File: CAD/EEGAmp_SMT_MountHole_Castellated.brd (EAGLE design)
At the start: 19.9 x 11.2 mm, 16 parts, among them U1 TL084QD

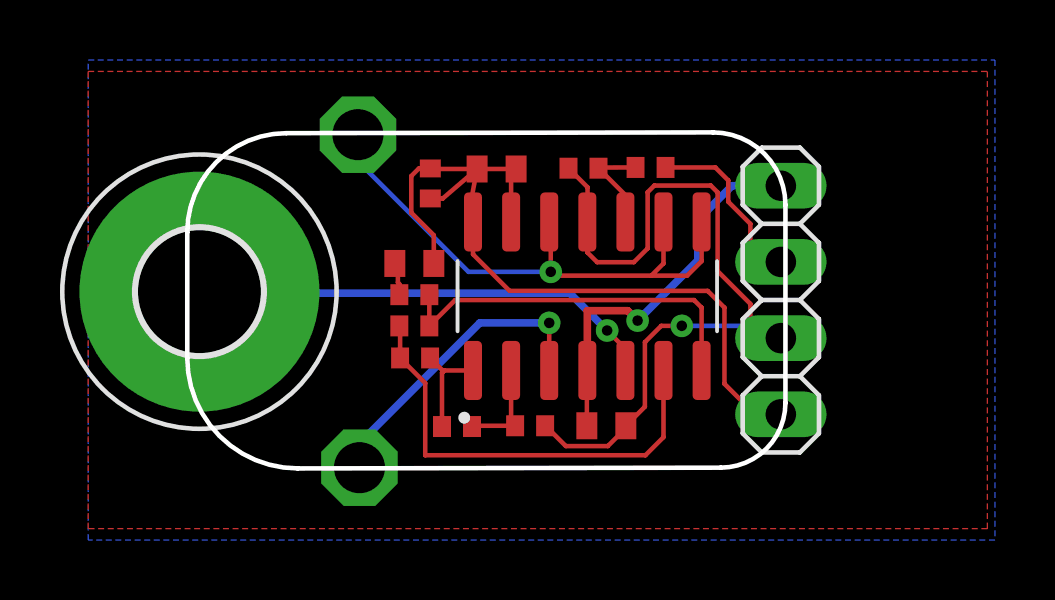
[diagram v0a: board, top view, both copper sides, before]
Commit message: added a filter cap on inputs
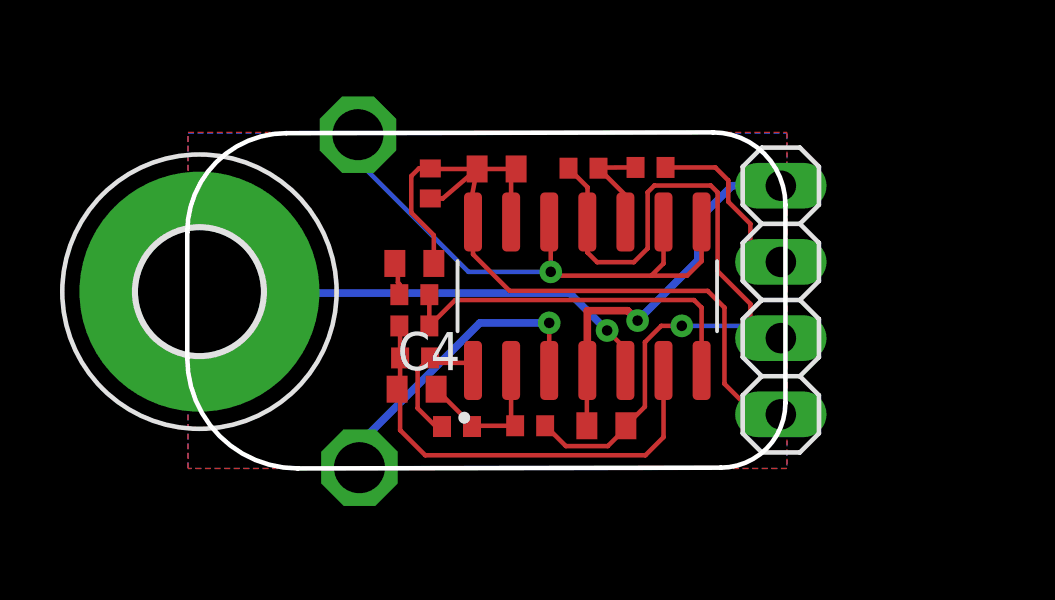
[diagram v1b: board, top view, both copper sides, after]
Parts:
- added C4: 2.2nF, rcl:C0402
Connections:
- net 1IN-: now also C4.2
- net 2IN-: now also C4.1
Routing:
- net 1IN-: track 3.36 -> 5.08 mm
- net 1OUT: track 3.49 -> 4.52 mm
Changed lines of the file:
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@@
 <attribute name="VALUE" x="26.7716" y="48.8188" size="0.0254" layer="27"/>
+</element>
+<element name="C4" library="rcl" library_urn="urn:adsk.eagle:library:334" package="C0402" package3d_urn="urn:adsk.eagle:package:23626/2" value="2.2nF" x="20.9804" y="22.3012" smashed="yes">
+<attribute name="NAME" x="20.3454" y="22.9362" size="1.27" layer="25"/>
+<attribute name="POPULARITY" value="16" x="20.9804" y="22.3012" size="1.778" layer="27" display="off"/>
+<attribute name="SPICEPREFIX" value="C" x="20.9804" y="22.3012" size="1.778" layer="27" display="off"/>
+<attribute name="VALUE" x="20.3454" y="20.3962" size="1.27" layer="27"/>
 </element>
 </elements>
@@
 <contactref element="JP2" pad="3"/>
 <polygon width="0.254" layer="16">
-<vertex x="40.259" y="33.274"/>
-<vertex x="40.259" y="17.272"/>
-<vertex x="10.033" y="17.272"/>
-<vertex x="10.033" y="33.274"/>
+<vertex x="33.3248" y="30.8356"/>
+<vertex x="33.3248" y="19.6596"/>
+<vertex x="13.3604" y="19.6596"/>
+<vertex x="13.3604" y="30.8356"/>
 </polygon>
 <polygon width="0.254" layer="1">
-<vertex x="10.033" y="32.893"/>
-<vertex x="40.005" y="32.893"/>
-<vertex x="40.005" y="17.653"/>
-<vertex x="10.033" y="17.653"/>
+<vertex x="13.3604" y="30.861"/>
+<vertex x="33.3248" y="30.861"/>
+<vertex x="33.3248" y="19.6596"/>
+<vertex x="13.3604" y="19.6596"/>
 </polygon>
 <wire x1="27.3536875" y1="20.4034" x2="25.9563125" y2="20.4034" width="0.1524" layer="1"/>
@@
 <wire x1="29.21" y1="22.925" x2="29.21" y2="20.701" width="0.1524" layer="1"/>
 <wire x1="28.6076" y1="20.0986" x2="21.2678" y2="20.0986" width="0.1524" layer="1"/>
-<wire x1="21.2678" y1="22.5044" x2="20.4296" y2="23.3426" width="0.1524" layer="1"/>
-<wire x1="21.2678" y1="22.5044" x2="21.2678" y2="20.0986" width="0.1524" layer="1"/>
+<wire x1="21.2678" y1="20.0986" x2="20.4296" y2="20.9368" width="0.1524" layer="1"/>
+<wire x1="20.4296" y1="20.9368" x2="20.4296" y2="23.3426" width="0.1524" layer="1"/>
 <wire x1="29.21" y1="20.701" x2="28.6076" y2="20.0986" width="0.1524" layer="1"/>
 <wire x1="20.4042" y1="24.4094" x2="20.4296" y2="24.384" width="0.1524" layer="1"/>
 <wire x1="20.4296" y1="24.384" x2="20.4296" y2="23.3426" width="0.1524" layer="1"/>
+<contactref element="C4" pad="1"/>
+<wire x1="20.3304" y1="22.3012" x2="20.4296" y2="23.3426" width="0" layer="19" extent="1-1"/>
 </signal>
 <signal name="3IN+">
@@
 <contactref element="R1" pad="1"/>
 <contactref element="R3" pad="2"/>
-<wire x1="21.898" y1="22.925" x2="22.86" y2="22.925" width="0.1524" layer="1"/>
-<wire x1="21.8266" y1="21.0566" x2="21.8266" y2="22.8536" width="0.1524" layer="1"/>
-<wire x1="21.8266" y1="22.8536" x2="21.8639" y2="22.8909" width="0.1524" layer="1"/>
-<wire x1="21.8639" y1="22.8909" x2="21.898" y2="22.925" width="0.1524" layer="1"/>
-<wire x1="21.4296" y1="23.3426" x2="21.8639" y2="22.9083" width="0.1524" layer="1"/>
-<wire x1="21.8639" y1="22.9083" x2="21.8639" y2="22.8909" width="0.1524" layer="1"/>
+<wire x1="22.606" y1="23.179" x2="22.86" y2="22.925" width="0.1524" layer="1"/>
+<wire x1="22.606" y1="23.179" x2="21.5932" y2="23.179" width="0.1524" layer="1"/>
+<wire x1="21.8266" y1="21.0566" x2="21.6234" y2="21.0566" width="0.1524" layer="1"/>
+<wire x1="21.6234" y1="21.0566" x2="21.0138" y2="21.6662" width="0.1524" layer="1"/>
+<wire x1="21.4296" y1="23.3426" x2="21.5932" y2="23.179" width="0.1524" layer="1"/>
+<wire x1="21.0138" y1="22.9268" x2="21.4296" y2="23.3426" width="0.1524" layer="1"/>
+<wire x1="21.0138" y1="21.6662" x2="21.0138" y2="22.9268" width="0.1524" layer="1"/>
 </signal>
 <signal name="VDD">
@@
 <wire x1="22.8266" y1="21.0566" x2="22.8266" y2="21.082" width="0.1524" layer="1"/>
 <wire x1="22.8266" y1="21.082" x2="24.265" y2="21.082" width="0.1524" layer="1"/>
+<contactref element="C4" pad="2"/>
+<wire x1="21.6304" y1="22.3012" x2="22.8266" y2="21.105" width="0.1524" layer="1"/>
+<wire x1="22.8266" y1="21.105" x2="22.8266" y2="21.082" width="0.1524" layer="1"/>
 </signal>
 <signal name="4IN-">
